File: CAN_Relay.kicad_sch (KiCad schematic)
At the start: 41 parts, among them J1 430450601, J4 691305340008, J5 691305340008, U1 Teensy4.0, U2 BTS716GB, U3 BTS716GB, U4 ADM3057EBRWZ, U5 LM22676MRE-5.0/NOPB

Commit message: added smd pins for teensy
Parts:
- added J2, J3: BCS-114-L-S-PE-BE, BCS:SAMTEC_BCS-114-L-S-PE-BE, symbol BCS-114-L-S-PE-BE:BCS-114-L-S-PE-BE
- renumbered U1 to #U1
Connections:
- net CANRX: now also J3.05
- net CANTX: now also J3.04
- net GND: now also J2.01, J3.02
- net at U3.3 (IN1): now also J2.10; no longer #U1.14 (12_MISO_MQSL)
- net at U3.4 (ST1/2): now also J2.09; no longer #U1.12 (10_CS_MQSR)
- net at U3.5 (IN2): now also J2.08; no longer #U1.11 (9_OUT1C)
- net at U3.7 (IN3): now also J2.07; no longer #U1.10 (8_TX2_IN1)
- net at U3.8 (ST3/4): now also J2.06; no longer #U1.9 (7_RX2_OUT1A)
- net at U3.9 (IN4): now also J2.05; no longer #U1.8 (6_OUT1D)
- net at U2.3 (IN1): now also J2.04; no longer #U1.7 (5_IN2)
- net at U2.4 (ST1/2): now also J2.03; no longer #U1.6 (4_BCLK2)
- net at U2.5 (IN2): now also J2.02; no longer #U1.5 (3_LRCLK2)
- net at U2.7 (IN3): no longer #U1.4 (2_OUT2)
- net at U2.8 (ST3/4): no longer #U1.3 (1_TX1_CTX2_MISO1)
- net at U2.9 (IN4): no longer #U1.2 (0_RX1_CRX2_CS1)
- new net +5V: J3.01
- no-connect marks 36 -> 50
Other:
- moved on the sheet: D1, D2, F1, J1, R3, R4

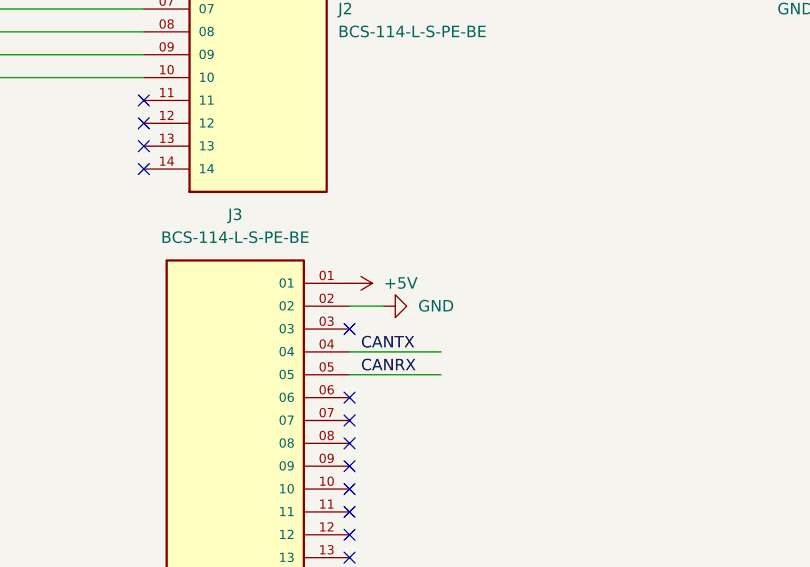
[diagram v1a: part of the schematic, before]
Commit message: wired all but relay outputs
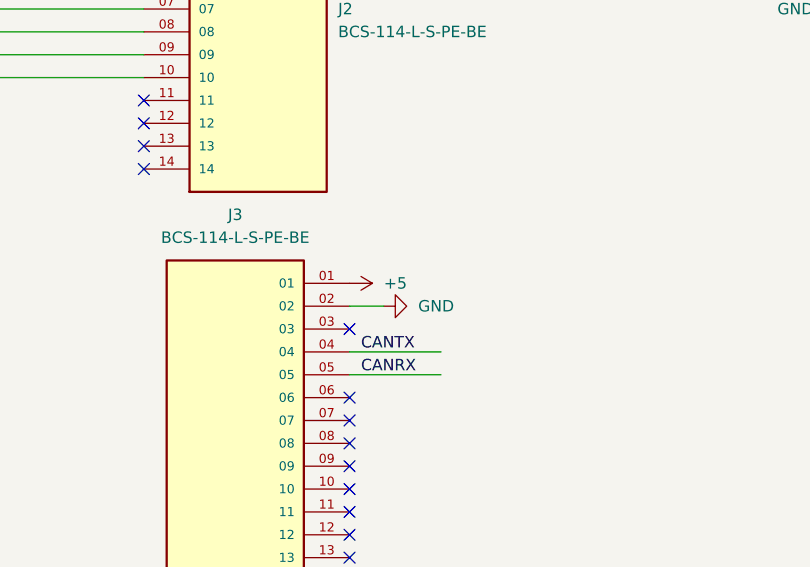
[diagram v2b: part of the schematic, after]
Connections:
- net +5V is gone; now on net +5: J3.01
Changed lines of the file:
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@@
 			)
 		)
-		(property "Value" "+5V"
+		(property "Value" "+5"
 			(at 205.74 101.5999 90)
 			(effects

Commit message: Complete with Errors
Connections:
- net GND: now also J4.1, J4.3, J4.5, J4.7, J5.1, J5.3, J5.5, J5.7; no longer J4.2, J4.4, J4.6, J4.8, J5.2, J5.4, J5.6, J5.8
- net at D10.1 (K), U2.18 (OUT1): now also J4.8; no longer J4.1
- net at D8.1 (K), U2.14 (OUT3): now also J4.4; no longer J4.5
- net at D3.1 (K), U3.13 (OUT4): now also J5.2; no longer J5.7
- net at D7.1 (K), U2.13 (OUT4): now also J4.2; no longer J4.7
- net at D4.1 (K), U3.14 (OUT3): now also J5.4; no longer J5.5
- net at D5.1 (K), U3.17 (OUT2): now also J5.6; no longer J5.3
- net at D6.1 (K), U3.18 (OUT1): now also J5.8; no longer J5.1
- net at D9.1 (K), U2.17 (OUT2): now also J4.6; no longer J4.3
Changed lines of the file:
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@@
 	(wire
 		(pts
-			(xy 49.53 127) (xy 53.34 127)
-		)
-		(stroke
-			(width 0)
-			(type default)
-		)
-	)
-	(wire
-		(pts
 			(xy 355.6 121.92) (xy 369.57 121.92)
 		)
@@
 	(wire
 		(pts
-			(xy 29.21 53.34) (xy 33.02 53.34)
-		)
-		(stroke
-			(width 0)
-			(type default)
-		)
-	)
-	(wire
-		(pts
 			(xy 157.48 139.7) (xy 125.73 139.7)
 		)
@@
 	(wire
 		(pts
+			(xy 49.53 127) (xy 53.34 127)
+		)
+		(stroke
+			(width 0)
+			(type default)
+		)
+	)
+	(wire
+		(pts
 			(xy 72.39 134.62) (xy 72.39 121.92)
 		)
@@
 	(wire
 		(pts
+			(xy 29.21 53.34) (xy 33.02 53.34)
+		)
+		(stroke
+			(width 0)
+			(type default)
+		)
+	)
+	(wire
+		(pts
 			(xy 179.07 78.74) (xy 162.56 78.74)
 		)
@@
 	(symbol
 		(lib_id "691305340008:691305340008")
-		(at 44.45 132.08 90)
+		(at 44.45 129.54 90)
+		(mirror x)
 		(unit 1)
 		(exclude_from_sim no)
@@
 		(on_board yes)
 		(dnp no)
-		(fields_autoplaced yes)
 		(property "Reference" "J5"
-			(at 45.72 115.57 90)
+			(at 43.18 129.5399 90)
 			(effects
 				(font
 					(size 1.27 1.27)
 				)
+				(justify left)
 			)
 		)
 		(property "Value" "691305340008"
-			(at 45.72 118.11 90)
+			(at 43.18 132.0799 90)
 			(effects
 				(font
 					(size 1.27 1.27)
 				)
+				(justify left)
 			)
 		)
 		(property "Footprint" "691305340008:691305340008"
-			(at 44.45 132.08 0)
+			(at 44.45 129.54 0)
 			(effects
 				(font
@@
 		)
 		(property "Datasheet" ""
-			(at 44.45 132.08 0)
+			(at 44.45 129.54 0)
 			(effects
 				(font
@@
 		)
 		(property "Description" ""
-			(at 44.45 132.08 0)
+			(at 44.45 129.54 0)
 			(effects
 				(font
@@
 		)
 		(property "MF" "Würth Elektronik"
-			(at 44.45 132.08 0)
+			(at 44.45 129.54 0)
 			(effects
 				(font
@@
 		)
 		(property "Description_1" "8 Position Terminal Block Header, Male Pins, Shrouded (4 Side) 0.150 (3.81mm) 90°, Right Angle - Through Hole"
-			(at 44.45 132.08 0)
+			(at 44.45 129.54 0)
 			(effects
 				(font
@@
 		)
 		(property "Package" "None"
-			(at 44.45 132.08 0)
+			(at 44.45 129.54 0)
 			(effects
 				(font
@@
 		)
 		(property "Price" "None"
-			(at 44.45 132.08 0)
+			(at 44.45 129.54 0)
 			(effects
 				(font
@@
 		)
 		(property "SnapEDA_Link" "https://www.snapeda.com/parts/691305340008/W%25C3%25BCrth+Elektronik+Midcom/view-part/?ref=snap"
-			(at 44.45 132.08 0)
+			(at 44.45 129.54 0)
 			(effects
 				(font
@@
 		)
 		(property "MP" "691305340008"
-			(at 44.45 132.08 0)
+			(at 44.45 129.54 0)
 			(effects
 				(font
@@
 		)
 		(property "Availability" "In Stock"
-			(at 44.45 132.08 0)
+			(at 44.45 129.54 0)
 			(effects
 				(font
@@
 		)
 		(property "Check_prices" "https://www.snapeda.com/parts/691305340008/W%25C3%25BCrth+Elektronik+Midcom/view-part/?ref=eda"
-			(at 44.45 132.08 0)
+			(at 44.45 129.54 0)
 			(effects
 				(font
@@
 	(symbol
 		(lib_id "691305340008:691305340008")
-		(at 24.13 58.42 90)
+		(at 24.13 55.88 90)
+		(mirror x)
 		(unit 1)
 		(exclude_from_sim no)
@@
 		(on_board yes)
 		(dnp no)
-		(fields_autoplaced yes)
 		(property "Reference" "J4"
-			(at 25.4 41.91 90)
+			(at 25.4 72.39 90)
 			(effects
 				(font
@@
 		)
 		(property "Value" "691305340008"
-			(at 25.4 44.45 90)
+			(at 25.4 69.85 90)
 			(effects
 				(font
@@
 		)
 		(property "Footprint" "691305340008:691305340008"
-			(at 24.13 58.42 0)
+			(at 24.13 55.88 0)
 			(effects
 				(font
@@
 		)
 		(property "Datasheet" ""
-			(at 24.13 58.42 0)
+			(at 24.13 55.88 0)
 			(effects
 				(font
@@
 		)
 		(property "Description" ""
-			(at 24.13 58.42 0)
+			(at 24.13 55.88 0)
 			(effects
 				(font
@@
 		)
 		(property "MF" "Würth Elektronik"
-			(at 24.13 58.42 0)
+			(at 24.13 55.88 0)
 			(effects
 				(font
@@
 		)
 		(property "Description_1" "8 Position Terminal Block Header, Male Pins, Shrouded (4 Side) 0.150 (3.81mm) 90°, Right Angle - Through Hole"
-			(at 24.13 58.42 0)
+			(at 24.13 55.88 0)
 			(effects
 				(font
@@
 		)
 		(property "Package" "None"
-			(at 24.13 58.42 0)
+			(at 24.13 55.88 0)
 			(effects
 				(font
@@
 		)
 		(property "Price" "None"
-			(at 24.13 58.42 0)
+			(at 24.13 55.88 0)
 			(effects
 				(font
@@
 		)
 		(property "SnapEDA_Link" "https://www.snapeda.com/parts/691305340008/W%25C3%25BCrth+Elektronik+Midcom/view-part/?ref=snap"
-			(at 24.13 58.42 0)
+			(at 24.13 55.88 0)
 			(effects
 				(font
@@
 		)
 		(property "MP" "691305340008"
-			(at 24.13 58.42 0)
+			(at 24.13 55.88 0)
 			(effects
 				(font
@@
 		)
 		(property "Availability" "In Stock"
-			(at 24.13 58.42 0)
+			(at 24.13 55.88 0)
 			(effects
 				(font
@@
 		)
 		(property "Check_prices" "https://www.snapeda.com/parts/691305340008/W%25C3%25BCrth+Elektronik+Midcom/view-part/?ref=eda"
-			(at 24.13 58.42 0)
+			(at 24.13 55.88 0)
 			(effects
 				(font

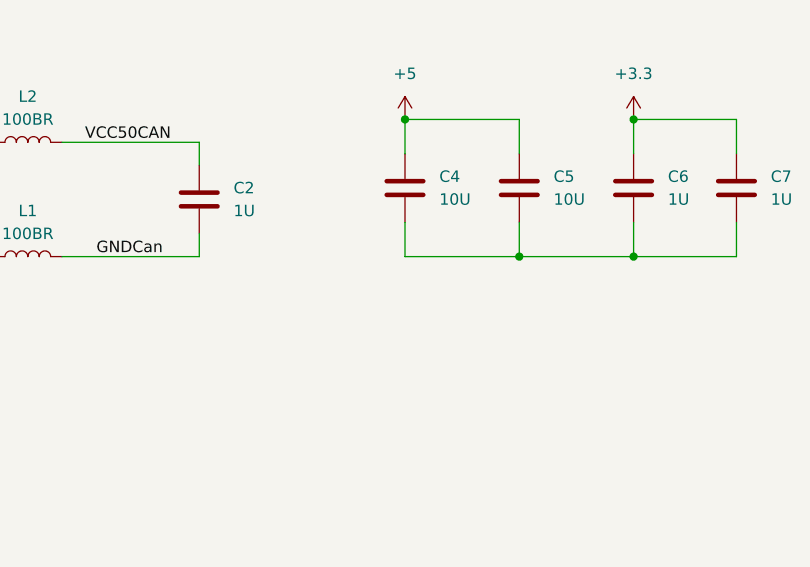
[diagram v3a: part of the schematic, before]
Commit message: fixed trace not being ground
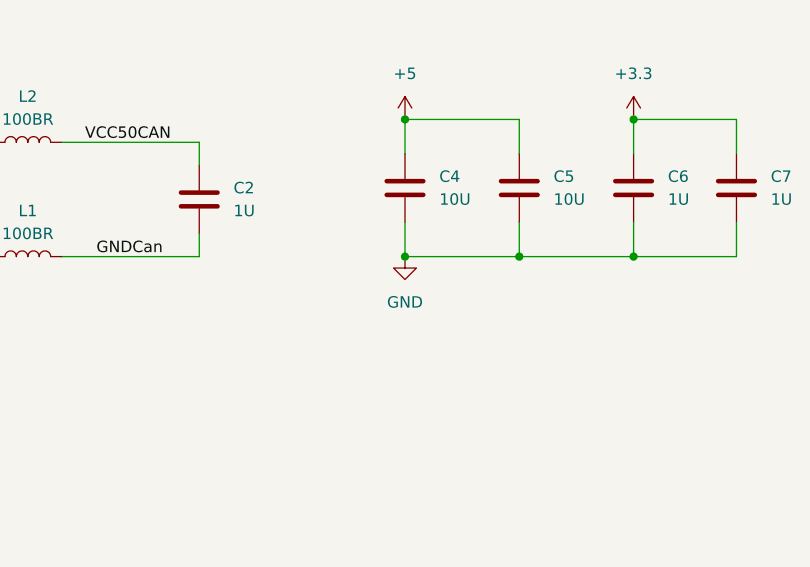
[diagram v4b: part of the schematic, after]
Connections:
- net GND: now also C4.2, C5.2, C6.2, C7.2
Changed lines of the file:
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@@
 	)
 	(junction
+		(at 340.36 185.42)
+		(diameter 0)
+		(color 0 0 0 0)
+	)
+	(junction
 		(at 67.31 129.54)
 		(diameter 0)
@@
 					(unit 1)
 				)
+			)
+		)
+	)
+	(symbol
+		(lib_id "power:GND")
+		(at 340.36 185.42 0)
+		(unit 1)
+		(exclude_from_sim no)
+		(in_bom yes)
+		(on_board yes)
+		(dnp no)
+		(fields_autoplaced yes)
+		(property "Reference" "#PWR027"
+			(at 340.36 191.77 0)
+			(effects
+				(font
+					(size 1.27 1.27)
+				)
+				(hide yes)
+			)
+		)
+		(property "Value" "GND"
+			(at 340.36 190.5 0)
+			(effects
+				(font
+					(size 1.27 1.27)
+				)
+			)
+		)
+		(property "Footprint" ""
+			(at 340.36 185.42 0)
+			(effects
+				(font
+					(size 1.27 1.27)
+				)
+				(hide yes)
+			)
+		)
+		(property "Datasheet" ""
+			(at 340.36 185.42 0)
+			(effects
+				(font
+					(size 1.27 1.27)
+				)
+				(hide yes)
+			)
+		)
+		(property "Description" "Power symbol creates a global label with name \"GND\" , ground"
+			(at 340.36 185.42 0)
+			(effects
+				(font
+					(size 1.27 1.27)
+				)
+				(hide yes)
+			)
+		)
+		(pin "1"
+		)
+		(instances
+			(project ""
+				(path "/5d5ade82-05d9-4966-a7df-afcf986d1e43"
+					(reference "#PWR027")
+					(unit 1)
+				)

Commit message: experimented with ground and power planes
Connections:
- net GND: now also U2.2 (GND1/2), U2.6 (GND3/4)
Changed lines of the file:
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@@
+	)
+	(junction
+		(at 114.3 45.72)
+		(diameter 0)
+		(color 0 0 0 0)
 	)
 	(junction
@@
 	(wire
 		(pts
+			(xy 114.3 45.72) (xy 114.3 60.96)
+		)
+		(stroke
+			(width 0)
+			(type default)
+		)
+	)
+	(wire
+		(pts
 			(xy 386.08 73.66) (xy 393.7 73.66)
 		)
@@
 	(wire
 		(pts
+			(xy 57.15 40.64) (xy 114.3 40.64)
+		)
+		(stroke
+			(width 0)
+			(type default)
+		)
+	)
+	(wire
+		(pts
 			(xy 391.16 44.45) (xy 391.16 38.1)
 		)
@@
 	(wire
 		(pts
-			(xy 114.3 60.96) (xy 114.3 45.72)
-		)
-		(stroke
+			(xy 114.3 40.64) (xy 114.3 45.72)
+		)
+		(stroke

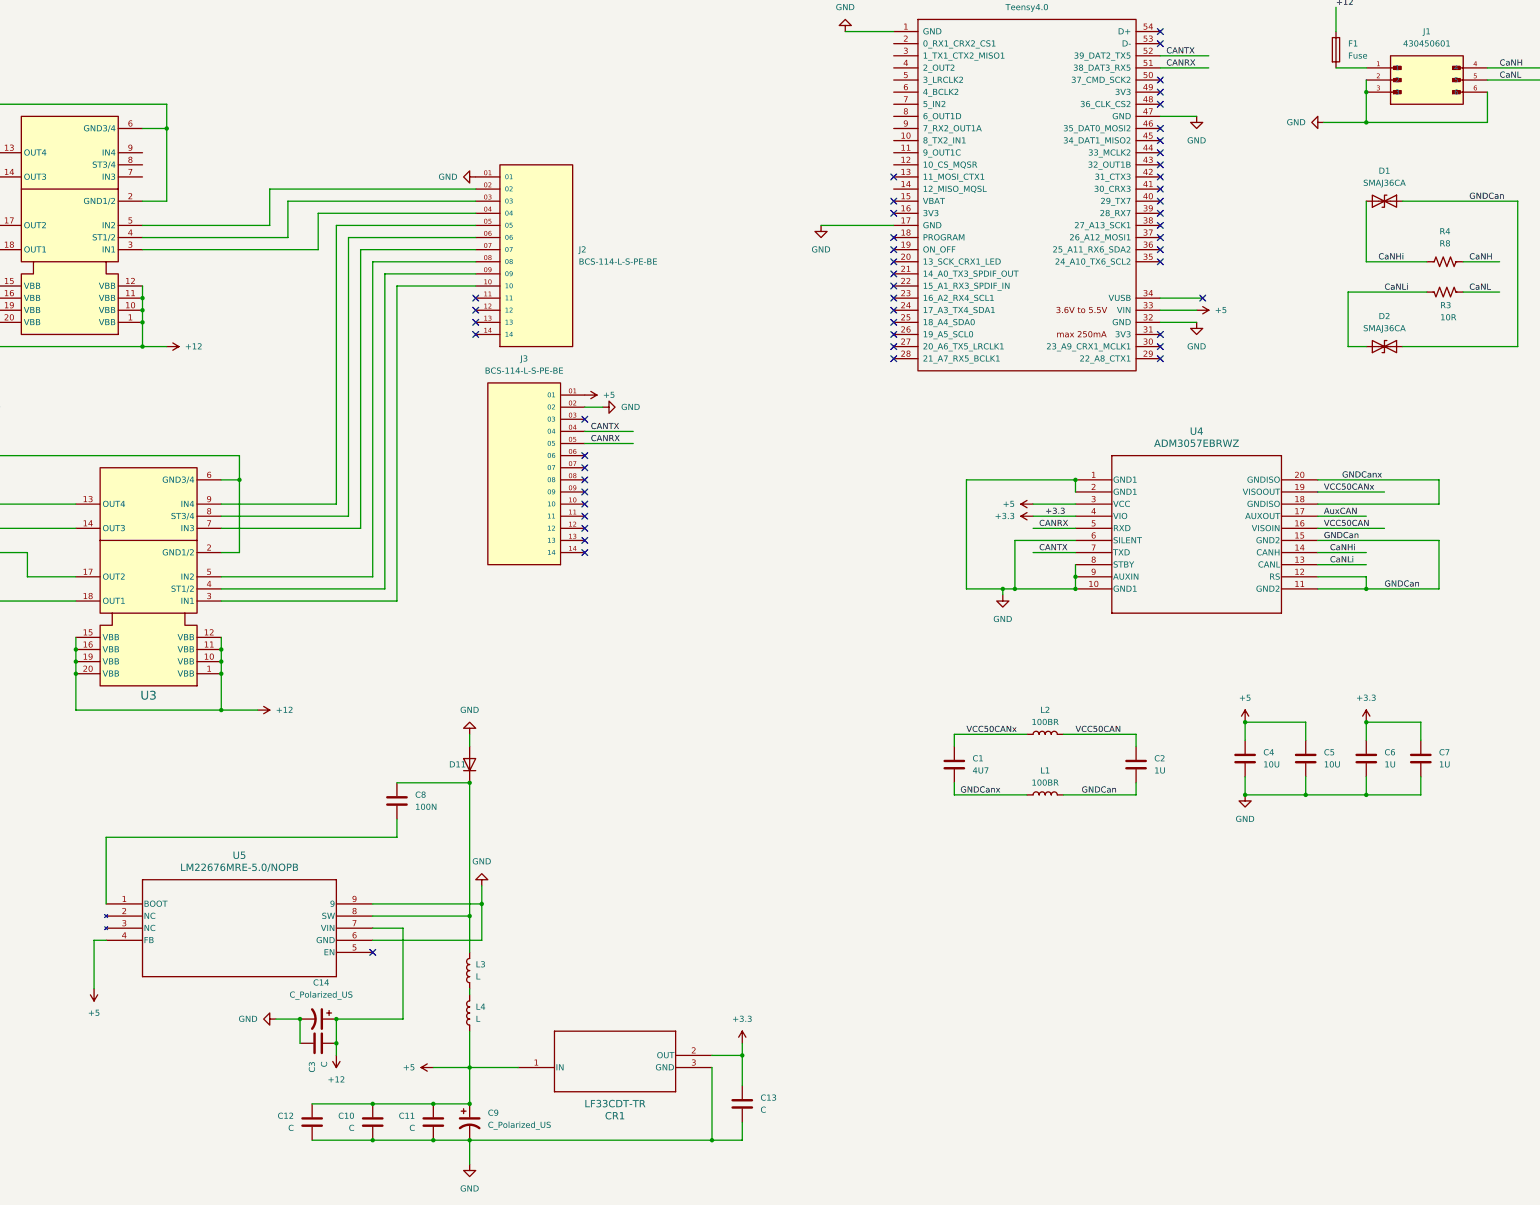
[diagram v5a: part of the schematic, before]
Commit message: Redid CAN side of PCB to replace Buck Converter
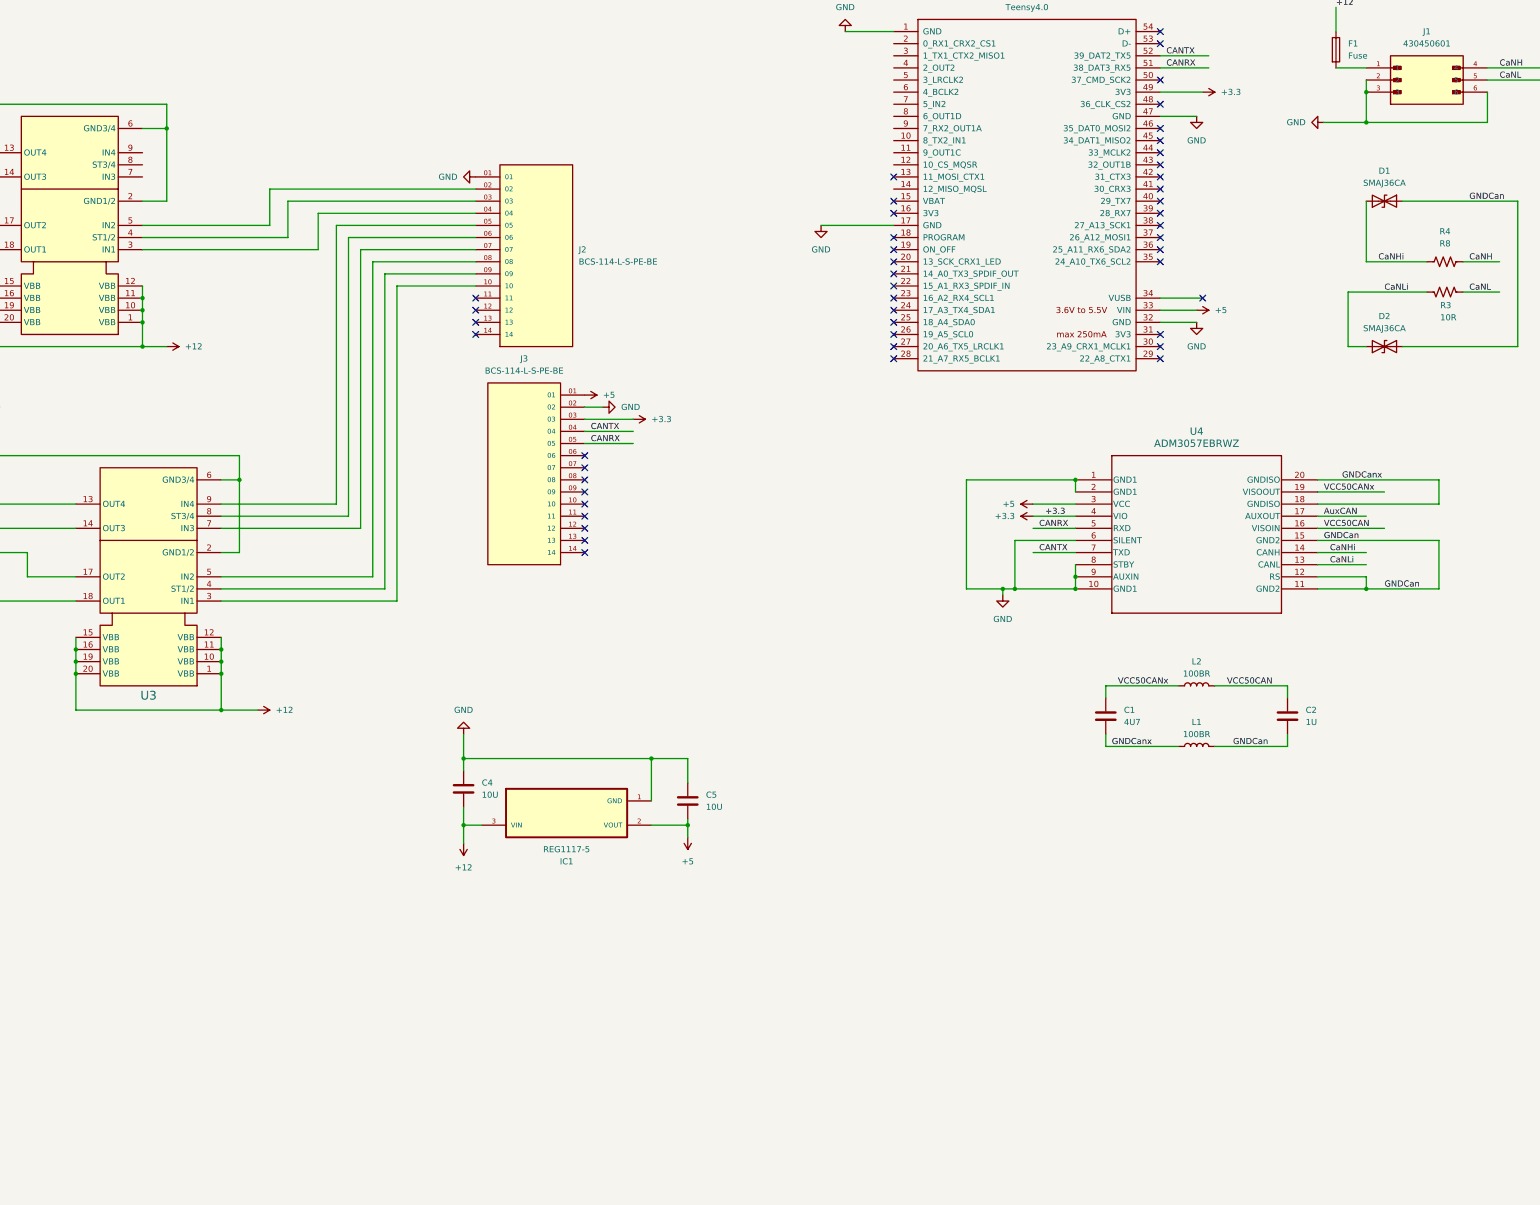
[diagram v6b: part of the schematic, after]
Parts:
- removed C10, C11, C12, C13, C3: C, Cap10U:CAPC2012X145N, symbol Device:C
- removed C14, C9: C_Polarized_US, EEEFT1V101AV:CAP_EEEFT1V101AV, symbol Device:C_Polarized_US
- removed C6, C7: 1U, GRT155C80J105KE01J:CAPC1005X55N, symbol Device:C
- removed C8: 100N, WCAP-CSGP_0402:WCAP-CSGP_0402, symbol Device:C
- removed CR1: LF33CDT-TR, LF33CDT-TR:TO228P972X240-3N, symbol 2025-07-13_05-52-55:LF33CDT-TR
- removed D11: D, RRE02VTM4SFHTR:DIO_RRE02VSM_ROM, symbol Device:D
- removed L3, L4: L, LQM18FN100M00D:INDC1608X90N, symbol Device:L
- removed U5: LM22676MRE-5.0/NOPB, LM22676MRE-5.0_NOPB:VREG_LM5017MR_NOPB, symbol 2025-07-13_05-49-35:LM22676MRE-5.0_NOPB
- added IC1: REG1117-5, REG1117-5:SOT230P700X180-4N, symbol REG1117-5:REG1117-5
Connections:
- net +12: now also C4.2, IC1.3 (VIN)
- net +3.3: now also #U1.49 (3V3), J3.03
- net +5: now also C5.2, IC1.2 (VOUT); no longer C4.1, C5.1
- net GND: now also C4.1, C5.1, IC1.1 (GND); no longer C4.2, C5.2
- no-connect marks 50 -> 47
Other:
- moved on the sheet: C1, C2, C4, C5, L1, L2
